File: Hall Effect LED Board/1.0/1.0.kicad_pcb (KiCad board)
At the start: 2 copper layers, 13 x 13.5 mm, 5 parts, among them J1 Conn_01x04_Pin

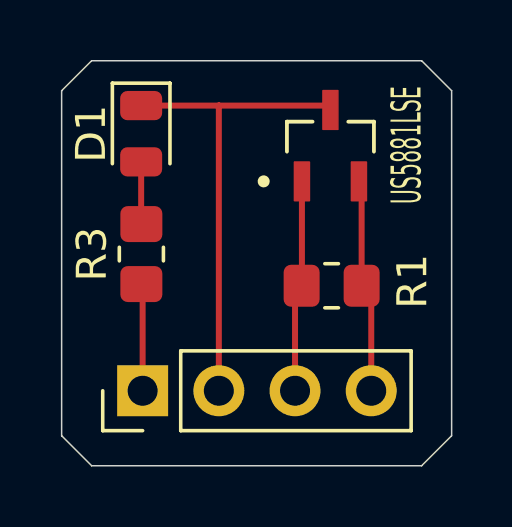
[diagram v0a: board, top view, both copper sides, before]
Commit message: Set relative project specific components
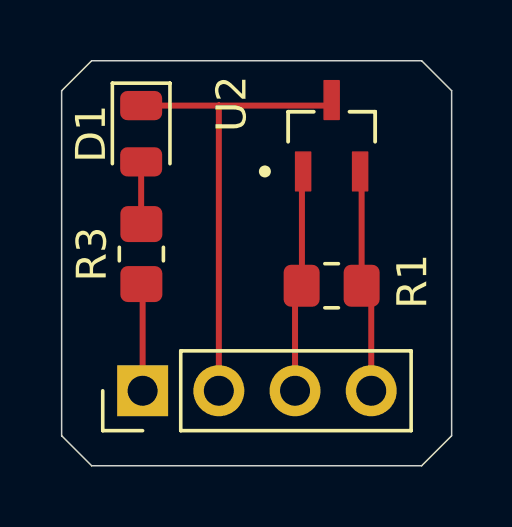
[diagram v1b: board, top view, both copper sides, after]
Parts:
- removed US5881LSE: US5881LSE-AAA-000-RE, US5881LSE-AAA-000-RE:SOT95P280X100-3N
- added U2: US5881LSE-AAA-000-RE, US5881LSE-AAA-000-RE:SOT95P280X100-3N, F.Cu at (158.5, 85.0)
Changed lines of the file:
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@@
 	(footprint "US5881LSE-AAA-000-RE:SOT95P280X100-3N"
 		(layer "F.Cu")
-		(at 158.459885 85.330592 90)
-		(property "Reference" "US5881LSE"
-			(at 0.016735 2.540115 90)
+		(at 158.5 85 90)
+		(property "Reference" "U2"
+			(at 1.065 -3.335 90)
 			(layer "F.SilkS")
 			(effects
 				(font
-					(size 1 0.5)
-					(thickness 0.125)
+					(size 1 1)
+					(thickness 0.15)
 				)
 			)
 		)
 		(property "Value" "US5881LSE-AAA-000-RE"
-			(at 3.330592 0.040115 0)
+			(at -3 5 90)
 			(layer "F.Fab")
 			(effects
 				(font
-					(size 0.7 0.5)
-					(thickness 0.125)
+					(size 1 1)
+					(thickness 0.15)
 				)
 			)
